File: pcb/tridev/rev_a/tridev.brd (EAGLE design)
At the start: 102.7 x 72.5 mm, 41 parts, among them J15 MICRO_USB_B_HIROSE_ZX62R-B-5P, J3 TC2030-JLINK-L, J4 TC2030-JLINK-L, U1 NRF51822QF, U2 TRIPOINT, U4 MAX8887EZK33+T, X1 EPSON-FA-128

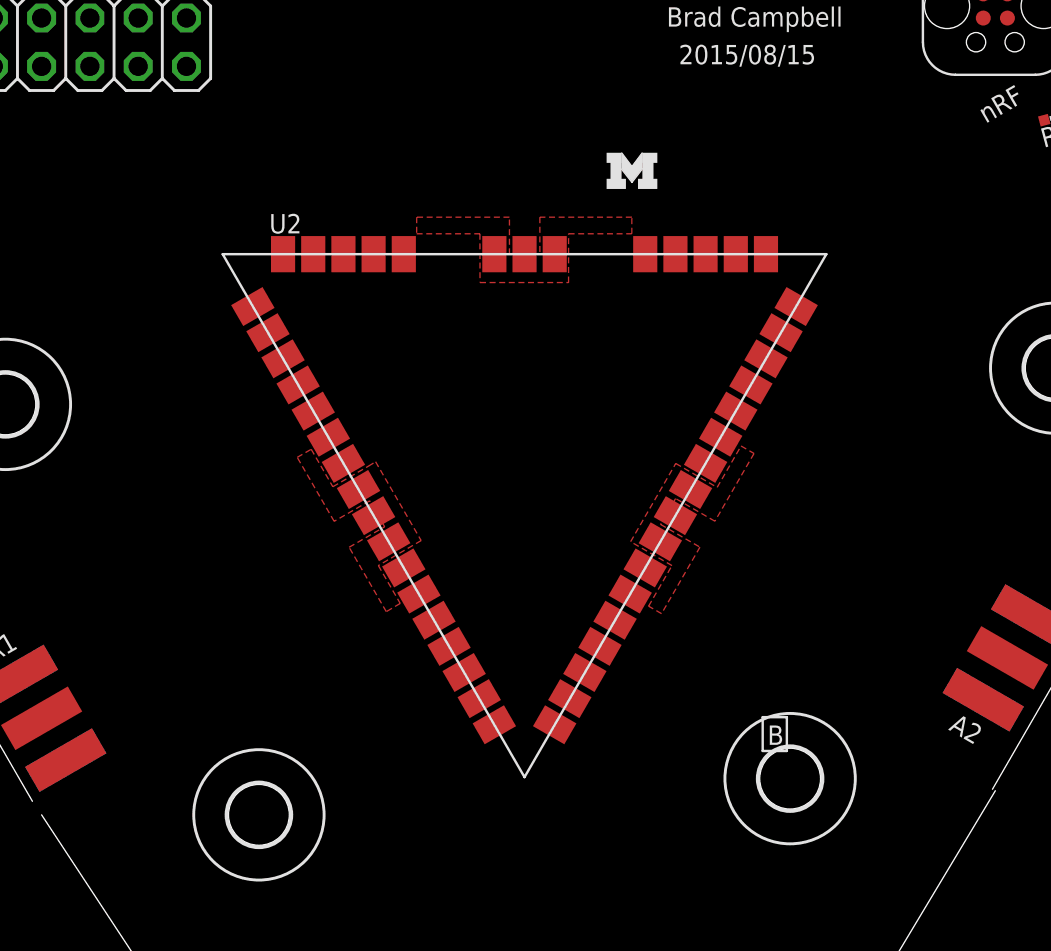
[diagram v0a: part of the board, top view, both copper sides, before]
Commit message: updated breakout
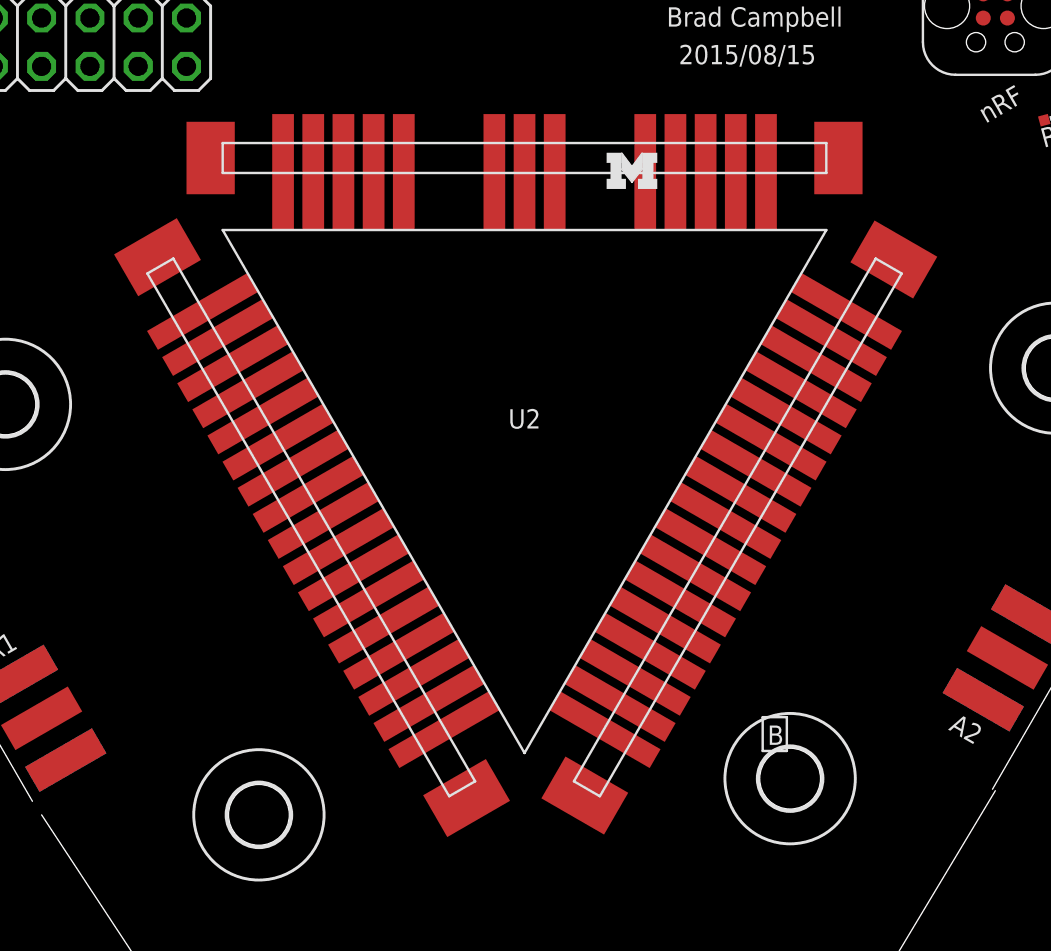
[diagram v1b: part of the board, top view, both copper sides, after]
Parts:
- U2: value TRIPOINT -> TRIPOINT-BREAKOUT; device tripoint:TRIPOINT -> tripoint:TRIPOINT-BREAKOUT
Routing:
- removed copper zone on layer 1, net GND

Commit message: breakout basically done
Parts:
- removed H5, H6, H7, H8: MOUNT-HOLE3.2, holes:3,2
- removed JP1: (no value), pinhead:2X10
- added C16, C17, C18, C19, C20, C22, C24, C25, C9: 0.1uF, passives:0402_CAP
- added C21, C23: 4.7uF, passives:CAP0603
- added C26, C27: 18pF, passives:0402_CAP
- added D3: RED, SparkFun-LED:LED-0603
- added D4: BLUE, SparkFun-LED:LED-0603
- added H1, H2, H3, H4: MOUNT-HOLE3.2, holes:3,2
- added J2: (no value), pinhead:2X10
- added J5, J6: (no value), SparkFun-Passives:1X02
- added L3, L4, L5: FERRITE_BEAD, passives:0603_CAP
- added R3: 12k 1%, passives:0402_RES
- added R7, R8: 1k, passives:0402_RES
- added U5: FT232HQ, chips:QFN-48-8MM
- added X2: TXC-8Z-12MHZ, crystals:TXC-8Z
- moved LOGO1 33.8 mm to (-26.7, -0.86)
- moved D2 21.6 mm to (27.9, 26.9), turned to 90 degrees
- moved C15 19.9 mm to (10.7, -34.0), turned to 270 degrees
- moved R1 19.7 mm to (27.9, 25.7), turned to 180 degrees
- moved C11 16.4 mm to (6.10, -34.0), turned to 270 degrees
- moved U4 16.2 mm to (8.38, -34.0), turned to 0 degrees
- moved R2 15.8 mm to (7.11, -42.4), turned to 180 degrees
- moved D1 15.6 mm to (7.11, -43.7), turned to 90 degrees
- moved C10 15.5 mm to (8.13, -37.6), turned to 270 degrees
- moved R5 10.7 mm to (20.1, 15.5), turned to 270 degrees
- moved R4 10.3 mm to (21.8, 15.5), turned to 270 degrees
- moved C13 9.42 mm to (6.86, -37.6), turned to 270 degrees
- moved J3 8.30 mm to (11.7, -24.1)
- moved R6 6.25 mm to (26.9, 10.1), turned to 135 degrees
- moved J4 5.08 mm to (19.7, 22.9)
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- renumbered J15 to J1
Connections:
- removed net DW_INT: U1.44, U2.38
- new net !DW_CS: J2.5, U2.23
- new net !DW_RST: J2.6, U2.24
- new net DW_CLK: J2.4, U2.22
- new net DW_IRQ: J2.15, U2.39
- new net DW_MISO: J2.3, U2.21
- new net DW_MOSI: J2.2, U2.20
- new net DW_SYNC: J2.1, U2.19
- new net DW_XTAL1: J2.16, U2.49
- new net N$12: C20.1, C21.POS, L5.2, U5.40
- new net N$13: C24.1, U5.38
- new net N$14: C26.1, U5.1, X2.3
- new net N$16: C27.1, U5.2, X2.1
- new net N$21: C25.1, U5.37
- new net N$22: R3.2, U5.5
- new net N$23: J5.2, U2.17
- new net N$24: D3.A, R7.1
- new net N$25: D4.A, R8.1
- new net N$26: D4.C, U5.17
- new net N$38: J2.17
- new net N$5: D3.C, U5.16
- new net NRF_VCC: C14.1, C8.1, J4.1, J6.2, R1.2, U1.1, U1.12
- new net TP_GPIO0: J2.7, U2.31
- new net TP_GPIO1: J2.8, U2.32
- new net TP_GPIO2: J2.9, U2.33
- new net TP_GPIO3: J2.10, U2.34
- new net TP_GPIO4: J2.11, U2.35
- new net TP_INT: J2.14, U1.44, U2.38
- new net USB_D+: J1.3, U5.7
- new net USB_D-: J1.2, U5.6
- new net VCC3V3: C16.1, C17.1, C22.1, C23.POS, C9.1, L3.2, L4.2, R7.2, R8.2, U5.12, U5.24, U5.34, U5.39, U5.46
- new net VPHY: C19.1, L3.1, U5.3
- new net VPLL: C18.1, L4.1, U5.8
- net GND: now also C16.2, C17.2, C18.2, C19.2, C20.2, C21.NEG, C22.2, C23.NEG, C24.2, C25.2, C26.2, C27.2, C9.2, J2.19, J2.20, R3.1, U5.10, U5.11, U5.22, U5.23, U5.35, U5.36, U5.4, U5.41, U5.42, U5.47, U5.48, U5.9, U5.PAD, X2.2, X2.4
- net I2C_SCL: now also J2.13, U5.13
- net I2C_SDA: now also J2.12, U5.14, U5.15
- net N$1: now also A1.ANT
- net N$2: now also A2.ANT
- net N$3: now also A3.ANT
- net VCC: now also J2.18, J5.1, J6.1; no longer C14.1, C8.1, J4.1, R1.2, U1.1, U1.12, U2.17
- net VUSB: now also L5.1
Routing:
- net I2C_SDA: track 0.00 -> 121.7 mm, vias 0 -> 4
- net I2C_SCL: track 0.00 -> 120.8 mm, vias 0 -> 5
- net VCC: track 18.6 -> 130.5 mm, vias 2 -> 3
- net TP_INT: track 0.00 -> 76.6 mm, vias 0 -> 2
- net DW_MOSI: track 0.00 -> 62.1 mm, vias 0 -> 1
- net DW_SYNC: track 0.00 -> 60.7 mm, vias 0 -> 1
- net DW_CLK: track 0.00 -> 60.0 mm, vias 0 -> 1
- net TP_GPIO1: track 0.00 -> 59.7 mm, vias 0 -> 1
- net TP_GPIO3: track 0.00 -> 58.9 mm, vias 0 -> 1
- net DW_MISO: track 0.00 -> 58.0 mm, vias 0 -> 1
- net !DW_RST: track 0.00 -> 57.9 mm, vias 0 -> 1
- net TP_GPIO0: track 0.00 -> 57.2 mm, vias 0 -> 1
- net NRF_VCC: track 0.00 -> 56.8 mm, vias 0 -> 2
- net TP_GPIO2: track 0.00 -> 56.2 mm, vias 0 -> 1
- net !DW_CS: track 0.00 -> 55.9 mm, vias 0 -> 1
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- added copper zone on layer 1, net GND
- added copper zone on layer 16, net GND
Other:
- board size 102.7 x 72.5 mm -> 108 x 72.4 mm
- board text added: "!CS"
- board text added: "!RST"
- board text added: "2015/10/04"
- board text added: "A"
- board text added: "CURR"
- board text added: "GND"
- board text added: "GP0"
- board text added: "GP1"
- board text added: "GP2"
- board text added: "GP3"
- board text added: "GP4"
- board text added: "INT"
- board text added: "IRQ"
- board text added: "MISO"
- board text added: "MOSI"
- board text added: "SCL"
- board text added: "SCLK"
- board text added: "SDA"
- board text added: "SYNC"
- board text added: "TriPoint"
- board text added: "VCC"
- board text added: "XTL1"
- board text removed: "2015/08/15"

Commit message: updated parts, added bom
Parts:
- removed C4: 1nF, passives:0402_CAP
- removed C5: 2.2nF, passives:0402_CAP
- removed U5: FT232HQ, chips:QFN-48-8MM
- added C44, C55: 18pF, passives:0402_CAP
- added U3: MAX8887EZK33+T, chips:SOT-23-5
- C10, C11, C14: value 4.7uF -> 0.1uF
- C12, C13: value 1uF -> 0.1uF
- C15: value 10nF -> 0.1uF
- C21: value 4.7uF -> 1uF; device passives:CAP0603 -> passives:0402_CAP
- C22: value 0.1uF -> 1uF
- C23: device passives:CAP0603 -> passives:0402_CAP
- C24, C25: value 0.1uF -> 4.7uF
- C26, C27: value 18pF -> 4.7uF; device passives:0402_CAP -> passives:CAP0603
- C6: value 47nF -> 1nF
- C7: value 0.1uF -> 2.2nF
- C8: value 0.1uF -> 10nF
- C9: value 0.1uF -> 47nF
- D3: value RED -> BLUE
- D4: value BLUE -> RED
- J3, J4: value TC2030-JLINK-L -> (none); device connector:TC2030-IDC -> SparkFun-Passives:1X02
- J5, J6: value (none) -> TC2030-JLINK-L; device SparkFun-Passives:1X02 -> connector:TC2030-IDC
- R3: value 12k 1% -> 1k
- R4: value 10k -> 1k
- R6: value 12k -> 10k
- R7: value 1k -> 12k
- R8: value 1k -> 12k 1%
- U1: value NRF51822QF -> TRIPOINT-BREAKOUT; device chips:QFN-48-6MM -> tripoint:TRIPOINT-BREAKOUT
- U2: value TRIPOINT-BREAKOUT -> NRF51822QF; device tripoint:TRIPOINT-BREAKOUT -> chips:QFN-48-6MM
- U4: value MAX8887EZK33+T -> FT232HQ; device chips:SOT-23-5 -> chips:QFN-48-8MM
- moved C9 66.3 mm to (40.4, 19.6), turned to 60 degrees
- moved C10 62.0 mm to (30.9, 20.1), turned to 150 degrees
- moved C21 59.9 mm to (33.5, 11.7), turned to 240 degrees
- moved C14 57.5 mm to (-10.9, -25.9), turned to 180 degrees
- moved C25 56.8 mm to (30.2, 14.3), turned to 240 degrees
- moved C12 55.8 mm to (0.70, -33.5), turned to 270 degrees
- moved J4 53.4 mm to (-10.8, -21.0), turned to 30 degrees
- moved C11 53.3 mm to (34.5, 11.1), turned to 240 degrees
- moved C8 51.0 mm to (10.7, -34.0), turned to 270 degrees
- moved R4 47.1 mm to (5.59, -28.7), turned to 0 degrees
- moved R7 45.7 mm to (26.9, 10.1), turned to 135 degrees
- moved U1 39.3 mm to (0.00, 0.00), turned to 0 degrees
- moved U2 39.3 mm to (35.6, 16.8), turned to 60 degrees
- moved J3 38.1 mm to (20.3, 13.0), turned to 0 degrees
- moved C15 23.4 mm to (-10.9, -24.9), turned to 180 degrees
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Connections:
- net !DW_CS: now also U1.23; no longer U2.23
- net !DW_RST: now also U1.24; no longer U2.24
- net AVDD: now also C21.1, C6.1, U2.35, U2.36; no longer C12.1, C4.1, U1.35, U1.36
- net BATIN: now also U2.5; no longer U1.5
- net DCC: now also U2.2; no longer U1.2
- net DW_CLK: now also U1.22; no longer U2.22
- net DW_IRQ: now also U1.39; no longer U2.39
- net DW_MISO: now also U1.21; no longer U2.21
- net DW_MOSI: now also U1.20; no longer U2.20
- net DW_SYNC: now also U1.19; no longer U2.19
- net DW_XTAL1: now also U1.49; no longer U2.49
- net GND: now also C21.2, C23.2, C26.NEG, C27.NEG, C44.2, C55.2, J5.5, J6.5, R7.1, R8.1, U1.10, U1.18, U1.25, U1.27, U1.42, U1.44, U1.8, U2.13, U2.33, U2.34, U2.GND, U3.2, U4.10, U4.11, U4.22, U4.23, U4.35, U4.36, U4.4, U4.41, U4.42, U4.47, U4.48, U4.9, U4.PAD; no longer C21.NEG, C23.NEG, C26.2, C27.2, C4.2, C5.2, J3.5, J4.5, R3.1, R6.1, U1.13, U1.33, U1.34, U1.GND, U2.10, U2.18, U2.25, U2.27, U2.42, U2.44, U2.8, U4.2, U5.10, U5.11, U5.22, U5.23, U5.35, U5.36, U5.4, U5.41, U5.42, U5.47, U5.48, U5.9, U5.PAD
- net I2C_SCL: now also U1.37, U2.47, U4.13; no longer U1.47, U2.37, U5.13
- net I2C_SDA: now also R6.1, U1.36, U2.48, U4.14, U4.15; no longer R4.1, U1.48, U2.36, U5.14, U5.15
- net N$1: now also U1.9; no longer U2.9
- net N$10: now also U2.38; no longer U1.38
- net N$11: now also C8.1, U3.4; no longer C15.1, U4.4
- net N$12: now also C26.POS, U4.40; no longer C21.POS, U5.40
- net N$13: now also C14.1, U4.38; no longer C24.1, U5.38
- net N$14: now also C55.1, U4.1; no longer C26.1, U5.1
- net N$15: now also C9.1, U2.29; no longer C6.1, U1.29
- net N$16: now also C44.1, U4.2; no longer C27.1, U5.2
- net N$17: now also C10.1, U2.39; no longer C7.1, U1.39
- net N$18: now also U2.31; no longer U1.31
- net N$19: now also U2.32; no longer U1.32
- net N$2: now also U1.26; no longer U2.26
- net N$20: now also C7.1, U2.30; no longer C5.1, U1.30
- net N$21: now also C15.1, U4.37; no longer C25.1, U5.37
- net N$22: now also R8.2, U4.5; no longer R3.2, U5.5
- net N$23: now also J4.2, U1.17; no longer J5.2, U2.17
- net N$24: now also D4.A, R3.1; no longer D3.A, R7.1
- net N$25: now also D3.A, R4.1; no longer D4.A, R8.1
- net N$26: now also D3.C, U4.17; no longer D4.C, U5.17
- net N$3: now also U1.43; no longer U2.43
- net N$4: now also J5.2, U1.28; no longer J3.2, U2.28
- net N$5: now also D4.C, U4.16; no longer D3.C, U5.16
- net N$6: now also U2.25; no longer U1.25
- net N$7: now also J5.4, U1.29; no longer J3.4, U2.29
- net N$8: now also J5.3, U1.30; no longer J3.3, U2.30
- net N$9: now also U2.37; no longer U1.37
- net NRF_VCC: now also C11.1, C25.1, J3.2, J6.1, U2.1, U2.12; no longer C14.1, C8.1, J4.1, J6.2, U1.1, U1.12
- net SWDCLK: now also J6.4, R7.2, U2.24; no longer J4.4, R6.2, U1.24
- net SWDIO/!RESET: now also J6.2, U2.23; no longer J4.2, U1.23
- net TP_GPIO0: now also U1.31; no longer U2.31
- net TP_GPIO1: now also U1.32; no longer U2.32
- net TP_GPIO2: now also U1.33; no longer U2.33
- net TP_GPIO3: now also U1.34; no longer U2.34
- net TP_GPIO4: now also U1.35; no longer U2.35
- net TP_INT: now also U1.38, U2.44; no longer U1.44, U2.38
- net USB_D+: now also U4.7; no longer U5.7
- net USB_D-: now also U4.6; no longer U5.6
- net VCC: now also C24.1, J4.1, R6.2, U3.5; no longer C11.1, J6.1, R4.2, U4.5
- net VCC3V3: now also C12.1, C13.1, C27.POS, R3.2, R4.2, U4.12, U4.24, U4.34, U4.39, U4.46; no longer C22.1, C23.POS, C9.1, R7.2, R8.2, U5.12, U5.24, U5.34, U5.39, U5.46
- net VPHY: now also U4.3; no longer U5.3
- net VPLL: now also U4.8; no longer U5.8
- net VUSB: now also C22.1, C23.1, U3.1, U3.3; no longer C10.1, C13.1, U4.1, U4.3
